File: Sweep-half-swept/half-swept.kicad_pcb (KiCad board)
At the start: 2 copper layers, 109 x 86.9 mm, 26 parts, among them J2 AudioJack4dpb, SW10 SW_Push, SW11 SW_Push, SW12 SW_Push, SW14 SW_Push, SW15 SW_Push, SW16 SW_Push, SW17 SW_Push, SW18 SW_Push, SW2 SW_Push, SW2 SW_SPDT, SW20 SW_Push, SW21 SW_Push, SW3 SW_Push, SW4 SW_Push, SW5 SW_Push, SW6 SW_Push, SW8 SW_Push, SW9 SW_Push, U1 ProMicro-kbd

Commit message: Update sweep half swept
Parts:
- removed RSW1: SW_Push, kbd:ResetSW
- removed the SW2 at (118.4, 46.2)
- added RSW2: SW_Push, * duckyb-collection:Tactile-Switch_SMT, F.Cu at (84.8, 22.3)
- POWER SW: moved to F.Cu
- SW1: renamed from SW2; footprint Kailh:SW_PG1350_rev_DPB -> * duckyb-collection:SW_PG1350_rev_DPB
- SW10: renamed from SW12; footprint Kailh:SW_PG1350_rev_DPB -> * duckyb-collection:SW_PG1350_rev_DPB
- SW11: renamed from SW14; footprint Kailh:SW_PG1350_rev_DPB -> * duckyb-collection:SW_PG1350_rev_DPB
- SW12: renamed from SW15; footprint Kailh:SW_PG1350_rev_DPB -> * duckyb-collection:SW_PG1350_rev_DPB
- SW13: renamed from SW16; footprint Kailh:SW_PG1350_rev_DPB -> * duckyb-collection:SW_PG1350_rev_DPB
- SW14: renamed from SW17; footprint Kailh:SW_PG1350_rev_DPB -> * duckyb-collection:SW_PG1350_rev_DPB
- SW15: renamed from SW18; footprint Kailh:SW_PG1350_rev_DPB -> * duckyb-collection:SW_PG1350_rev_DPB
- SW16: renamed from SW21; footprint Kailh:SW_PG1350_rev_DPB -> * duckyb-collection:SW_PG1350_rev_DPB
- SW17: renamed from SW20; footprint Kailh:SW_PG1350_rev_DPB -> * duckyb-collection:SW_PG1350_rev_DPB
- SW2: renamed from SW3; footprint Kailh:SW_PG1350_rev_DPB -> * duckyb-collection:SW_PG1350_rev_DPB
- SW3: renamed from SW4; footprint Kailh:SW_PG1350_rev_DPB -> * duckyb-collection:SW_PG1350_rev_DPB
- SW4: renamed from SW5; footprint Kailh:SW_PG1350_rev_DPB -> * duckyb-collection:SW_PG1350_rev_DPB
- SW5: renamed from SW6; footprint Kailh:SW_PG1350_rev_DPB -> * duckyb-collection:SW_PG1350_rev_DPB
- SW6: renamed from SW8; footprint Kailh:SW_PG1350_rev_DPB -> * duckyb-collection:SW_PG1350_rev_DPB
- SW7: renamed from SW9; footprint Kailh:SW_PG1350_rev_DPB -> * duckyb-collection:SW_PG1350_rev_DPB
- SW8: renamed from SW10; footprint Kailh:SW_PG1350_rev_DPB -> * duckyb-collection:SW_PG1350_rev_DPB
- SW9: renamed from SW11; footprint Kailh:SW_PG1350_rev_DPB -> * duckyb-collection:SW_PG1350_rev_DPB
- U1: footprint kbd:ProMicro_v2 -> * duckyb-collection:ProMicro_jumpers_facedown
- moved POWER SW 32.1 mm to (94.6, 24.6), turned to -15.5 degrees
- turned U1 to -90 degrees
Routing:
- net gnd: track 68.6 -> 15.1 mm, vias 0 -> 3
- net Switch11: track 160.7 -> 107.5 mm, vias 1 -> 0
- net Switch13: track 108.9 -> 58.5 mm, vias 1 -> 0
- net Switch12: track 129.9 -> 82.6 mm, vias 1 -> 0
- net Switch16: track 69.2 -> 24.6 mm, vias 1 -> 0
- net Switch14: track 87.8 -> 43.3 mm, vias 1 -> 0
- net Switch15: track 61.4 -> 18.6 mm, vias 1 -> 0
- net BT+_r: track 13.1 -> 50.6 mm, vias 1 -> 2
- net Switch1: track 137.5 -> 102.8 mm, vias 4 -> 1
- net Switch18: track 60.9 -> 34.4 mm
- net Switch17: track 43.1 -> 21.5 mm
- net reset: track 68.1 -> 49.7 mm, vias 0 -> 1
- net raw: track 24.7 -> 42.9 mm
- net Switch4: track 67.1 -> 49.1 mm, vias 1 -> 0
- net Switch8: track 79.2 -> 61.8 mm, vias 1 -> 0
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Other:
- net class Default removed
- board text added: "1) Place Pro-Micro with components facing DOWN"
- board text added: "2) Close JUMPER PADS on the OPPOSITE SIDE"
- board text removed: "Face down"
- board text removed: "POWER SW"

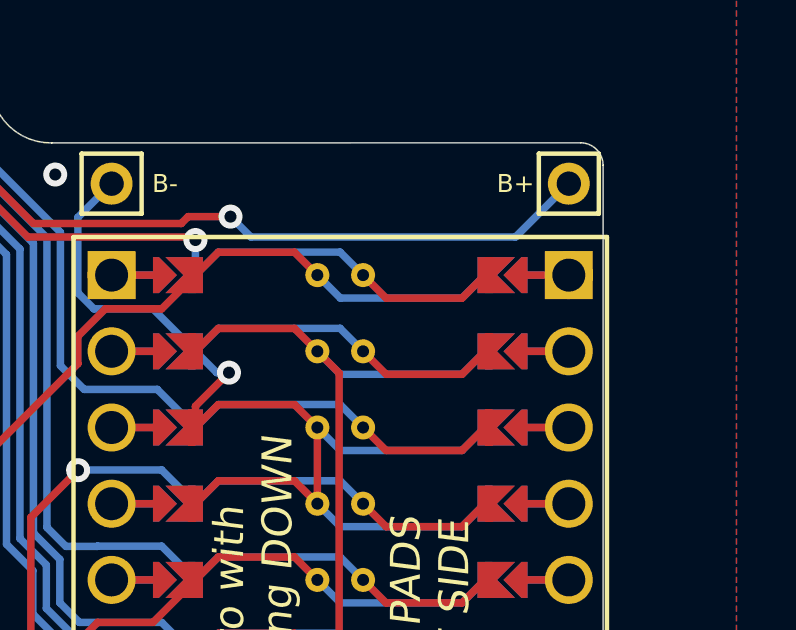
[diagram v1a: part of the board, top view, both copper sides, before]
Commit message: Add RAW/GND label, update gerber.zip
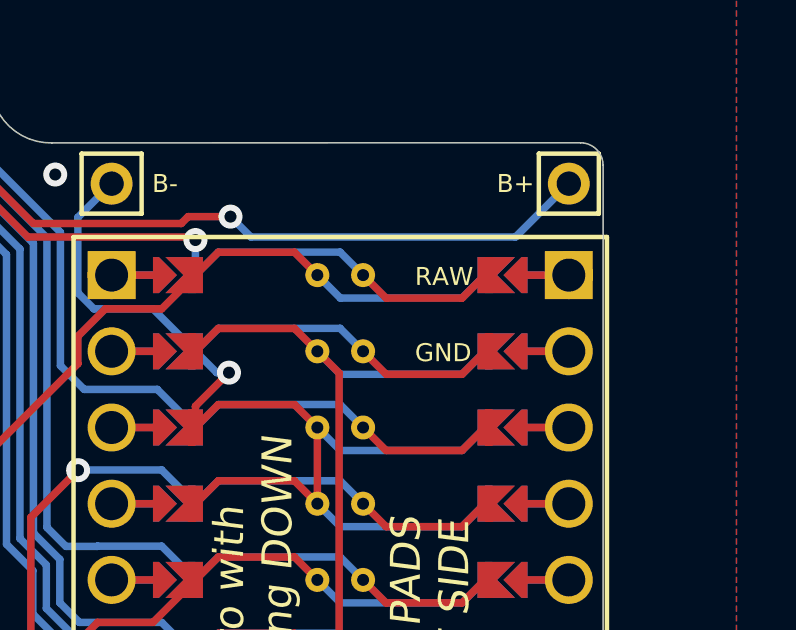
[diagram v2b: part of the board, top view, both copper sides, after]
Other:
- board text added: "GND"
- board text added: "RAW"
